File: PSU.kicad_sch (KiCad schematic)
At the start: 11 parts, among them U7 TPS631000DRLR

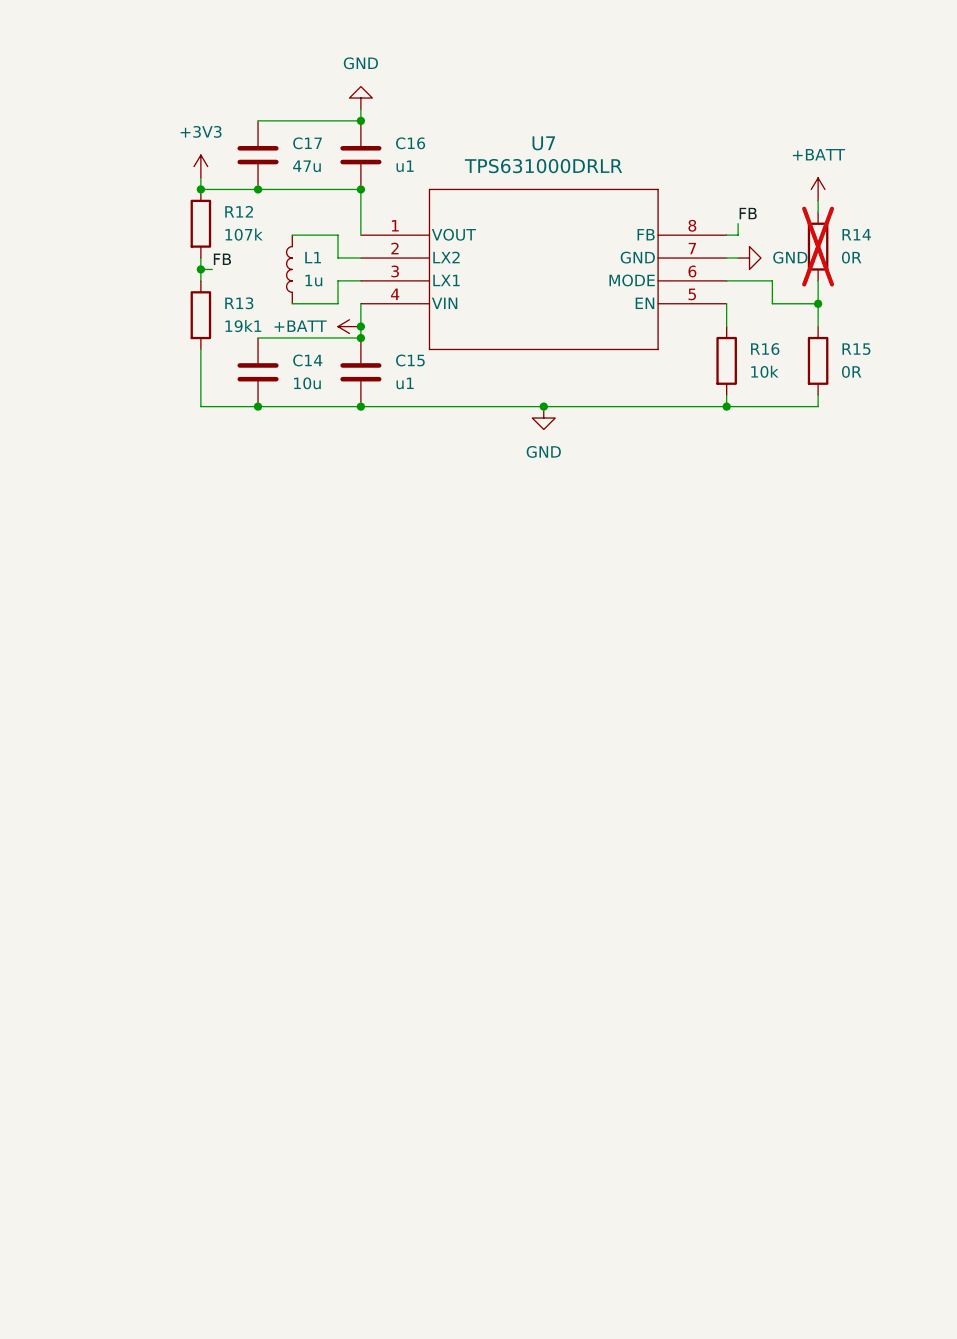
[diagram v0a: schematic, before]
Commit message: Finished PSU
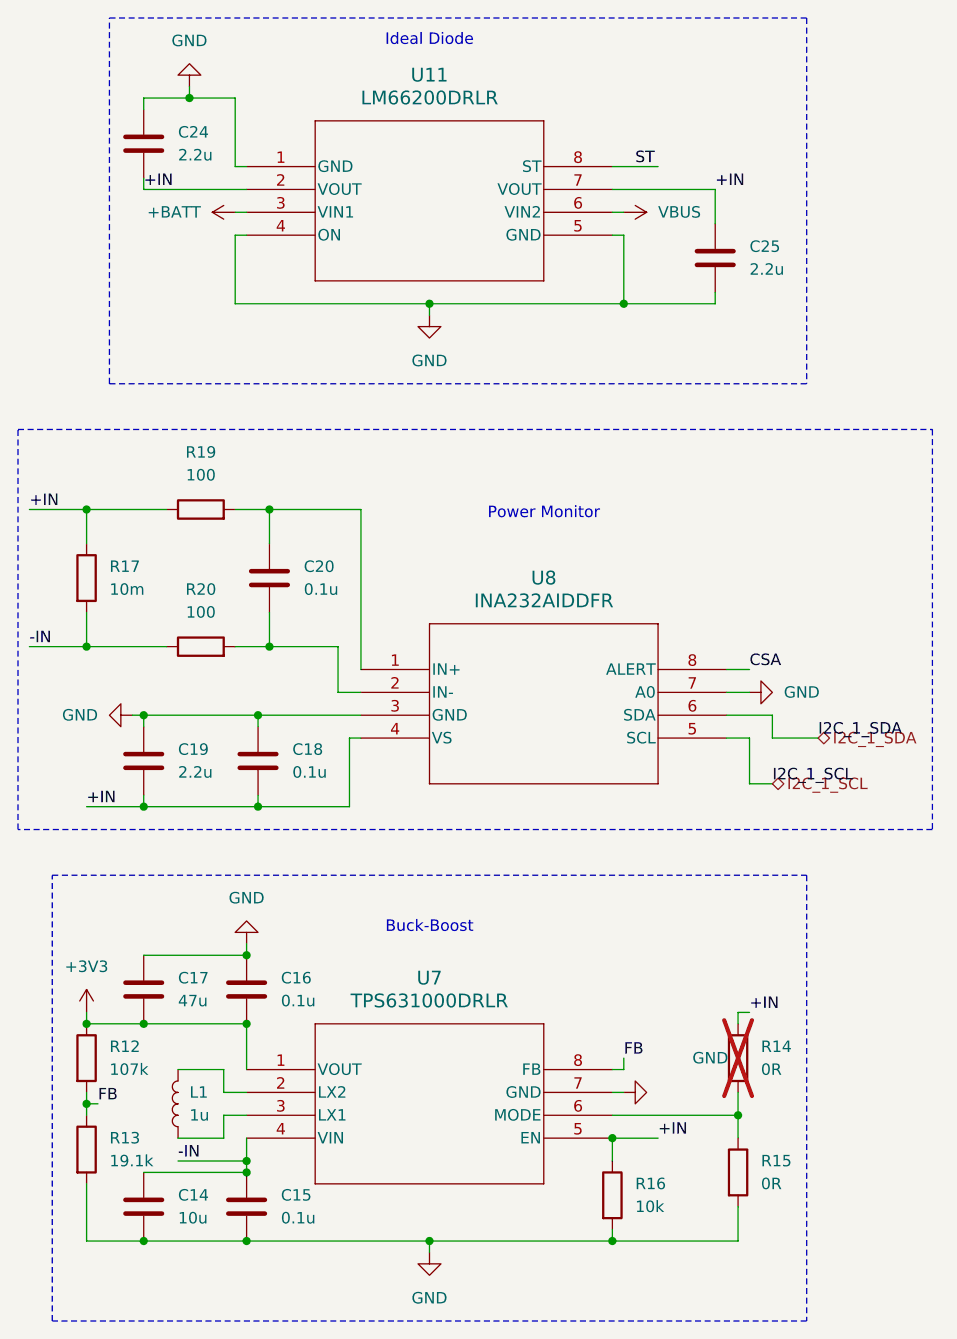
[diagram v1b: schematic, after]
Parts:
- added C18, C20: 0.1u, Capacitor_SMD:C_0603_1608Metric, symbol Device:C
- added C19, C24, C25: 2.2u, Capacitor_SMD:C_0603_1608Metric, symbol Device:C
- added R17: 10m, Resistor_SMD:R_0612_1632Metric, symbol Device:R
- added R19, R20: 100, Resistor_SMD:R_0603_1608Metric, symbol Device:R
- added U11: LM66200DRLR, LRI_partlib:LM66200, symbol LM66200:LM66200DRLR
- added U8: INA232AIDDFR, LRI_partlib:INA232AIDDFR, symbol INA232:INA232AIDDFR
- C15, C16: value u1 -> 0.1u
- R13: value 19k1 -> 19.1k
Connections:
- net +BATT: now also U11.3 (VIN1); no longer C14.1, C15.1, R14.1, U7.4 (VIN)
- net GND: now also C18.1, C19.1, C24.1, C25.2, U11.1 (GND), U11.4 (ON), U11.5 (GND), U8.3 (GND), U8.7 (A0)
- net +IN: now reaches R16.1, U7.5 (EN)
- net +IN: now also R14.1, C18.2, C19.2, C24.2, C25.1, R17.1, R19.1, U11.2 (VOUT), U11.7 (VOUT), U8.4 (VS)
- new net: C20.1, R19.2, U8.1 (IN+)
- new net: C20.2, R20.2, U8.2 (IN-)
- new net -IN: C14.1, C15.1, R17.2, R20.1, U7.4 (VIN)
- new net CSA: U8.8 (ALERT)
- new net I2C_1_SCL: U8.5 (SCL)
- new net I2C_1_SDA: U8.6 (SDA)
- new net ST: U11.8 (ST)
- new net VBUS: U11.6 (VIN2)
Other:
- note added: "Buck-Boost"
- note added: "Ideal Diode"
- note added: "Power Monitor"
- moved on the sheet: C14, C15, C16, C17, L1, R12, R13, R14, R15, R16, U7

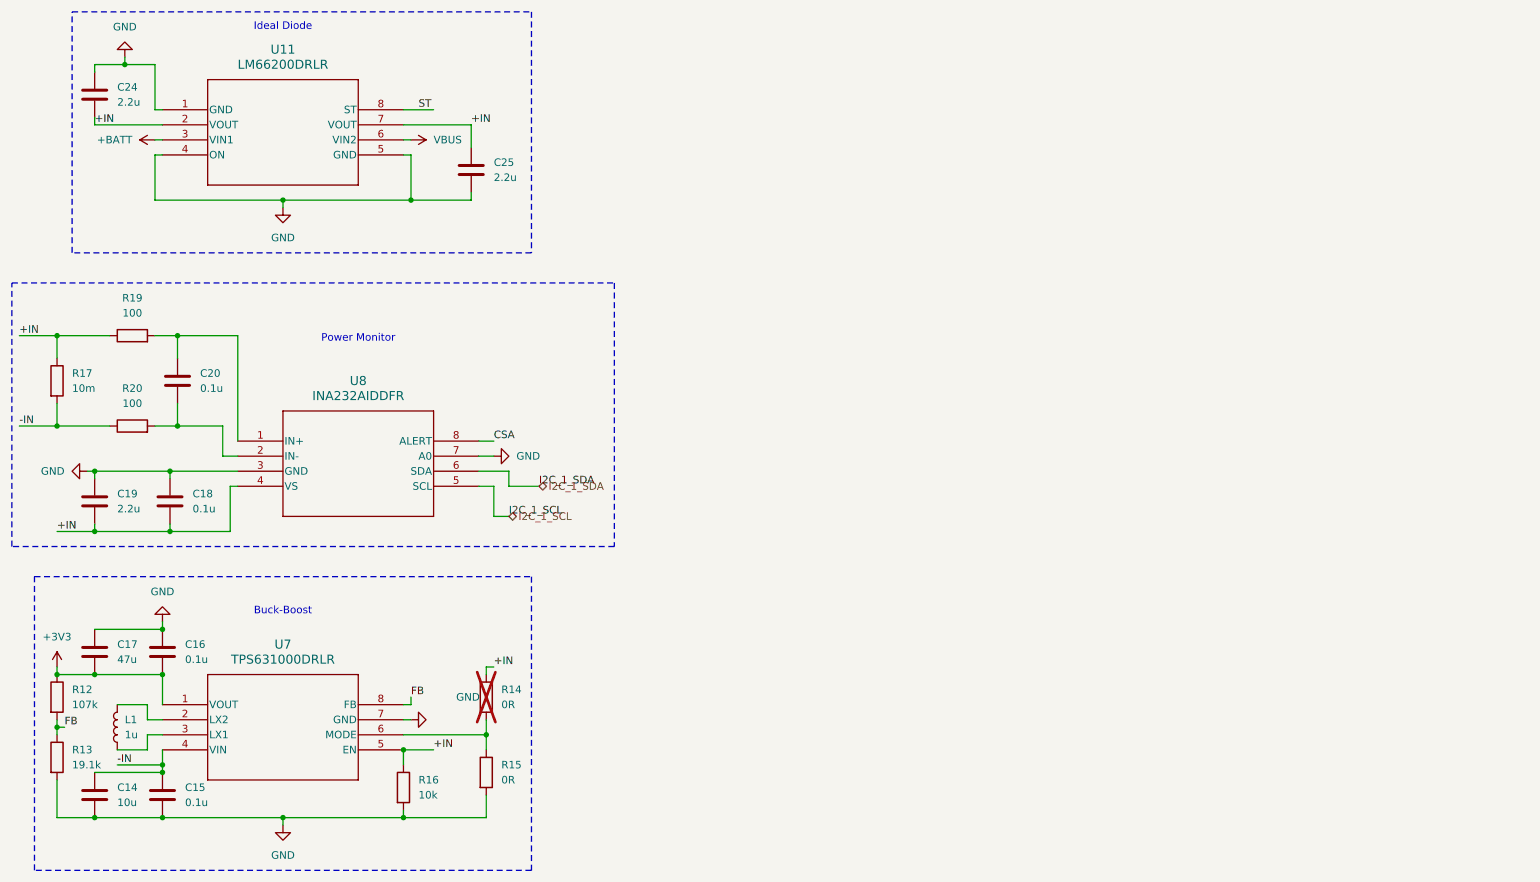
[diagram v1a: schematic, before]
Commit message: Added buttons, LEDs, TPs, and Miku
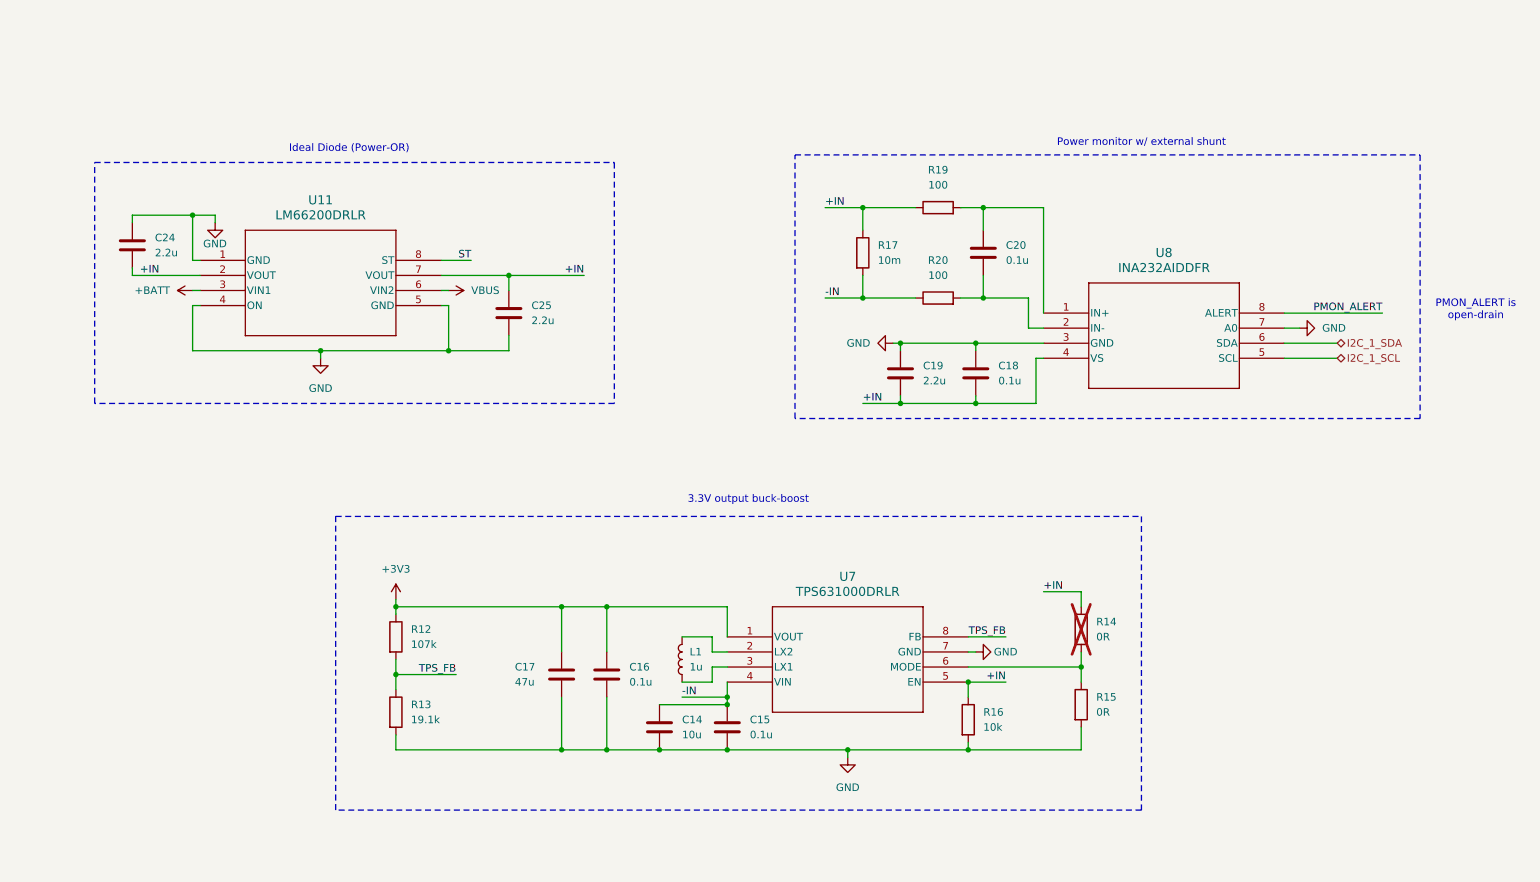
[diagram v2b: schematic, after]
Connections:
- net +3V3: now also C16.1, C17.1; no longer C16.2, C17.2
- net GND: now also C16.2, C17.2; no longer C16.1, C17.1
- net CSA renamed PMON_ALERT
- net FB renamed TPS_FB
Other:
- note added: "3.3V output buck-boost"
- note added: "Ideal Diode (Power-OR)"
- note added: "PMON_ALERT is open-drain"
- note added: "Power monitor w/ external shunt"
- note removed: "Buck-Boost"
- note removed: "Ideal Diode"
- note removed: "Power Monitor"
- moved on the sheet: C14, C15, C18, C19, C20, C24, C25, L1, R12, R13, R14, R15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

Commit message: Tentatively finished schematic
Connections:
- net ST renamed POR_ST
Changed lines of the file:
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@@
+	)
+	(junction
+		(at 191.77 140.97)
+		(diameter 0)
+		(color 0 0 0 0)
 	)
 	(junction
@@
 	(wire
 		(pts
+			(xy 191.77 124.46) (xy 191.77 140.97)
+		)
+		(stroke
+			(width 0)
+			(type default)
+		)
+	)
+	(wire
+		(pts
 			(xy 167.64 81.28) (xy 167.64 82.55)
 		)
@@
 	(wire
 		(pts
-			(xy 90.17 58.42) (xy 95.25 58.42)
+			(xy 90.17 58.42) (xy 99.06 58.42)
+		)
+		(stroke
+			(width 0)
+			(type default)
+		)
+	)
+	(wire
+		(pts
+			(xy 191.77 140.97) (xy 179.07 140.97)
+		)
+		(stroke
+			(width 0)
+			(type default)
+		)
+	)
+	(wire
+		(pts
+			(xy 234.95 69.85) (xy 232.41 69.85)
 		)
 		(stroke
@@
 	(wire
 		(pts
-			(xy 179.07 124.46) (xy 180.34 124.46)
+			(xy 179.07 124.46) (xy 191.77 124.46)
 		)
 		(stroke
@@
 	(wire
 		(pts
-			(xy 198.12 140.97) (xy 179.07 140.97)
-		)
-		(stroke
-			(width 0)
-			(type default)
-		)
-	)
-	(wire
-		(pts
 			(xy 191.77 49.53) (xy 191.77 67.31)
 		)
@@
 	(wire
 		(pts
-			(xy 232.41 69.85) (xy 234.95 69.85)
-		)
-		(stroke
-			(width 0)
-			(type default)
-		)
-	)
-	(wire
-		(pts
 			(xy 189.23 64.77) (xy 189.23 69.85)
 		)
@@
 	(wire
 		(pts
-			(xy 179.07 129.54) (xy 185.42 129.54)
+			(xy 179.07 129.54) (xy 186.69 129.54)
 		)
 		(stroke
@@
 	(wire
 		(pts
+			(xy 234.95 78.74) (xy 234.95 69.85)
+		)
+		(stroke
+			(width 0)
+			(type default)
+		)
+	)
+	(wire
+		(pts
 			(xy 161.29 49.53) (xy 170.18 49.53)
 		)
@@
 	(wire
 		(pts
-			(xy 179.07 121.92) (xy 185.42 121.92)
+			(xy 179.07 121.92) (xy 186.69 121.92)
 		)
 		(stroke
@@
 		(pts
 			(xy 232.41 74.93) (xy 241.3 74.93)
+		)
+		(stroke
+			(width 0)
+			(type default)
+		)
+	)
+	(wire
+		(pts
+			(xy 191.77 140.97) (xy 198.12 140.97)
 		)
 		(stroke
@@
 	)
 	(label "+IN"
-		(at 185.42 129.54 180)
+		(at 186.69 129.54 180)
 		(fields_autoplaced yes)
 		(effects
@@
 	)
 	(label "TPS_FB"
-		(at 185.42 121.92 180)
+		(at 186.69 121.92 180)
 		(fields_autoplaced yes)
 		(effects
@@
 		)
 	)
-	(label "ST"
-		(at 95.25 58.42 180)
+	(label "POR_ST"
+		(at 99.06 58.42 180)
 		(fields_autoplaced yes)
 		(effects
@@
 	(symbol
 		(lib_id "power:GND")
-		(at 234.95 69.85 90)
+		(at 234.95 78.74 0)
 		(unit 1)
 		(exclude_from_sim no)
@@
 		(fields_autoplaced yes)
 		(property "Reference" "#PWR038"
-			(at 241.3 69.85 0)
+			(at 234.95 85.09 0)
 			(effects
 				(font
@@
 		)
 		(property "Value" "GND"
-			(at 238.76 69.8499 90)
-			(effects
-				(font
-					(size 1.27 1.27)
-				)
-				(justify right)
+			(at 237.49 80.0099 0)
+			(effects
+				(font
+					(size 1.27 1.27)
+				)
+				(justify left)
 			)
 		)
 		(property "Footprint" ""
-			(at 234.95 69.85 0)
+			(at 234.95 78.74 0)
 			(effects
 				(font
@@
 		)
 		(property "Datasheet" ""
-			(at 234.95 69.85 0)
+			(at 234.95 78.74 0)
 			(effects
 				(font
@@
 		)
 		(property "Description" "Power symbol creates a global label with name \"GND\" , ground"
-			(at 234.95 69.85 0)
+			(at 234.95 78.74 0)
 			(effects
 				(font
@@
 					(unit 1)
 				)
-			)
-		)
-	)
-	(symbol
-		(lib_id "power:GND")
-		(at 180.34 124.46 90)
-		(unit 1)
-		(exclude_from_sim no)
-		(in_bom yes)
-		(on_board yes)
-		(dnp no)
-		(property "Reference" "#PWR032"
-			(at 186.69 124.46 0)
-			(effects
-				(font
-					(size 1.27 1.27)
-				)
-				(hide yes)
-			)
-		)
-		(property "Value" "GND"
-			(at 183.388 124.46 90)
-			(effects
-				(font
-					(size 1.27 1.27)
-				)
-				(justify right)
-			)
-		)
-		(property "Footprint" ""
-			(at 180.34 124.46 0)
-			(effects
-				(font
-					(size 1.27 1.27)
-				)
-				(hide yes)
-			)
-		)
-		(property "Datasheet" ""
-			(at 180.34 124.46 0)
-			(effects
-				(font
-					(size 1.27 1.27)
-				)
-				(hide yes)
-			)
-		)
-		(property "Description" "Power symbol creates a global label with name \"GND\" , ground"
-			(at 180.34 124.46 0)
-			(effects
-				(font
-					(size 1.27 1.27)
-				)
-				(hide yes)
-			)
-		)
-		(pin "1"
-		)
-		(instances
-			(project "flight-computer-lite"
-				(path "/68fb1519-f2e0-49f5-8b7c-4cc7366600ef/c9638264-4233-4dd7-8ba7-e3ef28adbc94"
-					(reference "#PWR032")
-					(unit 1)
-				)

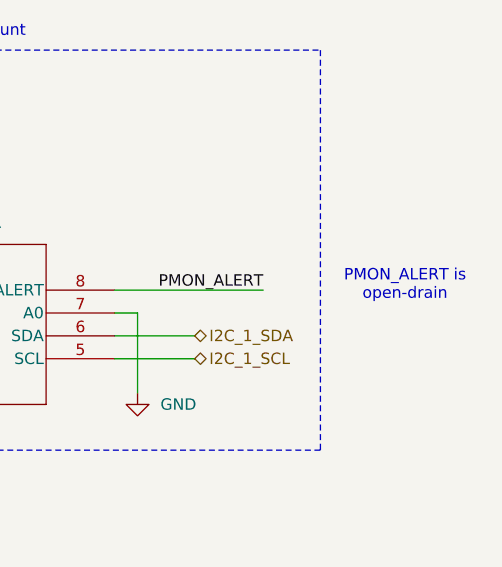
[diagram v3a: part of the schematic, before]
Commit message: Added I2C resistor values
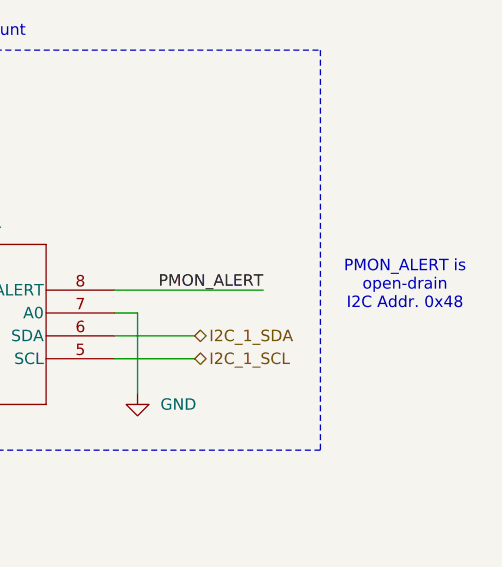
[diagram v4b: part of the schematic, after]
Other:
- note added: "PMON_ALERT is open-drain I2C Addr. 0x48"
- note removed: "PMON_ALERT is open-drain"
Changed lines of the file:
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@@
 		)
 	)
-	(text "PMON_ALERT is\nopen-drain"
+	(text "PMON_ALERT is\nopen-drain\nI2C Addr. 0x48"
 		(exclude_from_sim no)
 		(at 264.668 66.802 0)

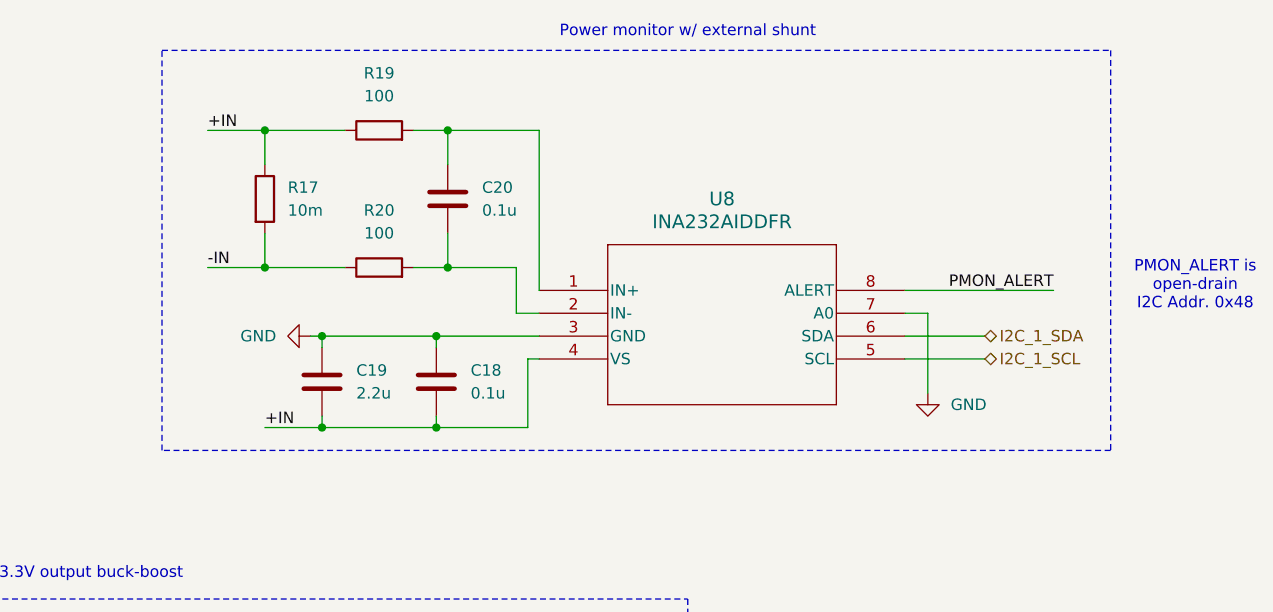
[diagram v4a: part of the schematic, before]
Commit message: Routed PSU
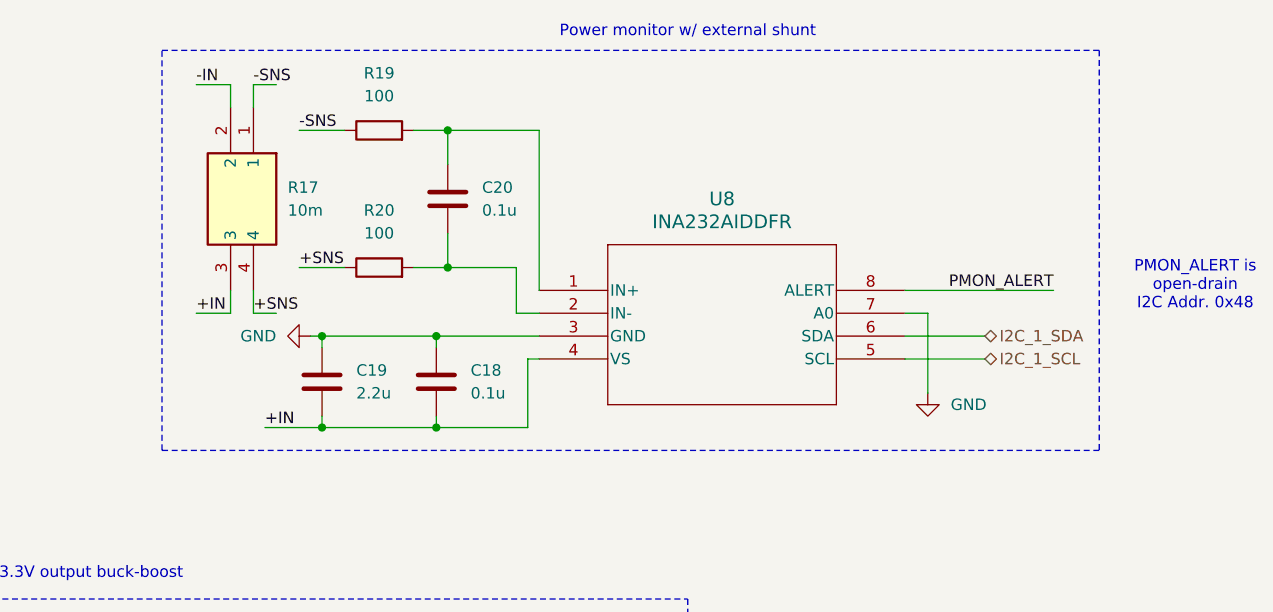
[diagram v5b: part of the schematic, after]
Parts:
- removed R17: 10m, Resistor_SMD:R_0612_1632Metric, symbol Device:R
- added R17: 10m, LRI_partlib:L4CA0612L0M50FNR, symbol L4CA0612LR010FNR:L4CA0612LR010FNR
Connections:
- net +IN: now also R17.3; no longer R19.1
- net -IN: now also R17.2; no longer R20.1
- new net +SNS: R17.4, R20.1
- new net -SNS: R17.1, R19.1

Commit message: major routing update!
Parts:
- R12: value 107k -> 107K
- R13: value 19.1k -> 19.1K
- R16: value 10k -> 10K
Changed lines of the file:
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@@
 			)
 		)
-		(property "Value" "10k"
+		(property "Value" "10K"
 			(at 181.61 137.1599 0)
 			(effects
@@
 			)
 		)
-		(property "Value" "19.1k"
+		(property "Value" "19.1K"
 			(at 85.09 135.8899 0)
 			(effects
@@
 			)
 		)
-		(property "Value" "107k"
+		(property "Value" "107K"
 			(at 85.09 123.1899 0)
 			(effects
